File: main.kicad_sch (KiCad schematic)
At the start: 165 parts, among them J1 USB_C_Receptacle_USB2.0_16P, J3 Barrel_Jack_MountingPin, Q1 STL6P3LLH6, Q2 STL6P3LLH6, SW1 TS-1088-AR02016, SW2 TS-1088-AR02016, U1 STUSB4500QTR, U10 INA180A2, U11 INA180A2, U12 INA180A2, U13 INA180A2, U2 LMR16030PDDAR, U3 W25Q128JVS, U5 PCF8575DBR, U6 TPS55289RYQR, U7 ESP32-C3, U8 TPS55289RYQR, U9 AP1117-33, Y1 X322540MPB4SI

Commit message: Schematics done
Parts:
- removed C10, C11, C9: 1uF, Capacitor_SMD:C_0402_1005Metric, symbol Device:C
- removed R7, R8: 100K, PCM_Resistor_SMD_AKL:R_0402_1005Metric, symbol Device:R
- removed TP1: TestPoint, TestPoint:TestPoint_Pad_D1.5mm, symbol Connector:TestPoint
- removed U1: STUSB4500QTR, Package_DFN_QFN:QFN-24-1EP_4x4mm_P0.5mm_EP2.7x2.7mm, symbol Interface_USB:STUSB4500QTR
- removed U5: PCF8575DBR, Package_SO:SSOP-24_5.3x8.2mm_P0.65mm, symbol Interface_Expansion:PCF8575DBR
- added C65, C70, C71: 22uF, Capacitor_SMD:C_0805_2012Metric, symbol Device:C
- added C66, C67, C68: 1uF, Capacitor_SMD:C_0402_1005Metric, symbol Device:C
- added C69, C72: 100nF, Capacitor_SMD:C_0402_1005Metric, symbol Device:C
- added C73, C74: 47uF, Capacitor_SMD:C_0805_2012Metric, symbol Device:C
- added C75, C79, C81: 1uF, Capacitor_SMD:C_0201_0603Metric, symbol Device:C
- added C76, C78, C80, C82: 100nF, Capacitor_SMD:C_0201_0603Metric, symbol Device:C
- added C77: 10uF, Capacitor_SMD:C_0402_1005Metric, symbol Device:C
- added D1, D12, D13, D14, D15, D16, D17, D3: SMBJ40CA, PCM_Diode_SMD_AKL:D_SMB_TVS, symbol PCM_Diode_TVS_AKL:SMBJ40CA
- added D11: SS34, Diode_SMD:D_SMA, symbol PCM_Diode_Schottky_AKL:SS34
- added F1, F6: SL1210650, Fuse:Fuse_1210_3225Metric, symbol Device:Polyfuse
- added F2: SL1210650, symbol Device:Polyfuse
- added F3, F4, F5: SMD1812P350TF, Fuse:Fuse_1812_4532Metric, symbol Device:Polyfuse
- added J4: Conn_01x07_Pin, Connector_PinHeader_1.27mm:PinHeader_1x07_P1.27mm_Vertical, symbol Connector:Conn_01x07_Pin
- added J5: Conn_01x04_Pin, Connector_PinSocket_2.54mm:PinSocket_1x04_P2.54mm_Vertical, symbol Connector:Conn_01x04_Pin
- added J6, J7, J8: Conn_01x11_Pin, Connector_PinHeader_1.27mm:PinHeader_1x11_P1.27mm_Vertical, symbol Connector:Conn_01x11_Pin
- added L6: IHLP4040DZER100M01, Inductor_SMD:L_APV_APH1040, symbol Device:L
- added L7: 2nH, Inductor_SMD:L_0402_1005Metric, symbol Device:L
- added R51: 499, PCM_Resistor_SMD_AKL:R_0201_0603Metric, symbol Device:R
- added R52, R53, R58: 100K, PCM_Resistor_SMD_AKL:R_0402_1005Metric, symbol Device:R
- added R54, R55, R56: 0, PCM_Resistor_SMD_AKL:R_0201_0603Metric, symbol Device:R
- added R57: 49.9K, PCM_Resistor_SMD_AKL:R_0402_1005Metric, symbol Device:R
- added R59: 16.9K, PCM_Resistor_SMD_AKL:R_0402_1005Metric, symbol Device:R
- added R60: 0.01, PCM_Resistor_SMD_AKL:R_0402_1005Metric, symbol Device:R
- added TP17, TP18, TP19, TP20, TP21, TP22, TP23, TP24, TP25: TestPoint, TestPoint:TestPoint_Pad_D1.5mm, symbol Connector:TestPoint
- added TP26, TP27: TestPoint, TestPoint:TestPoint_power, symbol Connector:TestPoint
- added U14: LMR16030PDDAR, LMR16030:LMR16030, symbol LMR16030SDDAR:LMR16030PDDAR
- added U4: PCA9555PW, Package_SO:TSSOP-24_4.4x7.8mm_P0.65mm, symbol Interface_Expansion:PCA9555PW
- added U5: STUSB4500QTR, Package_DFN_QFN:QFN-24-1EP_4x4mm_P0.5mm_EP2.7x2.7mm, symbol Interface_USB:STUSB4500QTR
- J1: value USB_C_Receptacle_USB2.0_16P -> TYPE-C-31-M-31
- J3: value Barrel_Jack_MountingPin -> DC-005-5A-2.5-SMT
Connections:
- net +3.3V_LDO: now also U7.11 (VDD3P3_RTC), U7.17 (VDD3P3_CPU), U7.18 (VDD_SPI), U7.31 (VDDA), U7.32 (VDDA), C69.1, C76.1, C77.1, C78.1, C79.1, C80.1, C81.1, C82.1, J5.1 (Pin_1), J7.1 (Pin_1), J7.10 (Pin_10), J7.11 (Pin_11), J7.2 (Pin_2), J7.3 (Pin_3), J7.4 (Pin_4), J7.5 (Pin_5), J7.6 (Pin_6), J7.7 (Pin_7), J7.8 (Pin_8), J7.9 (Pin_9), L7.1, TP22.1, U4.24 (VDD)
- net +5.2V: now also F4.1; no longer C47.1, TP10.1, U13.4 (-), U9.3 (VI)
- net +5.2V_: now also C65.1, J4.6 (Pin_6); no longer C43.1, C44.1, L3.2, R20.1, R23.1, U13.3 (+)
- net +5V_USB: now also D16.2 (A)
- net DISH: now also U5.9 (DISCH)
- net Earth: now also J3.MP (MountPin), C65.2, C66.2, C67.2, C68.2, C69.2, C70.2, C71.2, C73.2, C74.2, C75.2, C76.2, C77.2, C78.2, C79.2, C80.2, C81.2, C82.2, D1.1 (K), D11.2 (A), D12.1 (K), D13.1 (K), D14.1 (K), D15.1 (K), D16.1 (K), D17.1 (K), D3.1 (K), J4.7 (Pin_7), J5.4 (Pin_4), J8.1 (Pin_1), J8.10 (Pin_10), J8.11 (Pin_11), J8.2 (Pin_2), J8.3 (Pin_3), J8.4 (Pin_4), J8.5 (Pin_5), J8.6 (Pin_6), J8.7 (Pin_7), J8.8 (Pin_8), J8.9 (Pin_9), R52.2, R53.2, R54.1, R55.1, R56.1, R57.2, R59.2, TP21.1, TP27.1, U14.7 (GND), U14.9 (EP), U4.12 (VSS), U5.10 (GND), U5.22 (VSYS), U5.25 (GND), U5.3 (NC)
- net LDO_EN: now also U4.7 (IO0_3)
- net PD-RST: now also U4.6 (IO0_2), U5.6 (RESET)
- net PD-Voltage: now also C70.1, C71.1, D17.2 (A), F6.1, U14.2 (VIN), U14.3 (EN); no longer TP15.1
- net PD_VDD: now also C68.1, U5.24 (VDD)
- net SCL: now also TP18.1, U4.22 (SCL), U5.7 (SCL)
- net SDA: now also TP17.1, U4.23 (SDA), U5.8 (SDA)
- net SPI_MOSI: now also J4.4 (Pin_4), TP19.1
- net SPI_SCLK: now also J4.5 (Pin_5), TP20.1
- net ST7789_CS: now also J4.1 (Pin_1)
- net ST7789_DC: now also J4.2 (Pin_2)
- net TPS1_EN: now also U4.4 (IO0_0)
- net TPS2_EN: now also U4.5 (IO0_1)
- net U0RX: now also J5.2 (Pin_2)
- net U0TX: now also R51.2
- net VBUS_EN_SNK: now also U5.16 (VBUS_EN_SNK)
- net VBUS_VS_DISH: now also U5.18 (VBUS_VS_DISCH)
- net VOUT1: now also F1.1; no longer TP7.1
- net VOUT2: now also F2.1; no longer TP8.1
- net VOUT3: now also F3.1; no longer TP9.1
- net at D4.1 (L1), J1.A5 (CC1): now also U5.1 (CC1DB), U5.2 (CC1)
- net at D4.3 (L2), J1.B5 (CC2): now also U5.4 (CC2), U5.5 (CC2DB)
- net at U7.2 (VDD3P3): now also U7.3 (VDD3P3), C75.1, L7.2
- new net: D13.2 (A), F4.2, TP10.1
- new net: C66.1, U5.23 (VREG_2V7)
- new net: R58.2, R59.1, U14.5 (FB)
- new net: D14.2 (A), F5.2, TP26.1
- new net: C43.1, C44.1, L3.2, R20.1, R23.1
- new net: C67.1, U5.21 (VREG_1V2)
- new net: C72.1, U14.1 (BOOT)
- new net: C72.2, D11.1 (K), L6.1, U14.8 (SW)
- new net: D3.2 (A), F2.2, TP8.1
- new net: TP24.1, U4.1 (~{INT})
- new net: R52.1, U5.12 (ADDR0)
- new net: R53.1, U5.13 (ADDR1)
- new net: TP23.1, U5.19 (ALERT)
- new net: R55.2, U4.2 (A1)
- new net: R57.1, U14.4 (RT/SYNC)
- new net: D12.2 (A), F3.2, TP9.1
- new net: R56.2, U4.21 (A0)
- new net: D15.2 (A), F6.2, TP15.1
- new net: TP25.1, U14.6 (PG)
- new net: J5.3 (Pin_3), R51.1
- new net: R54.2, U4.3 (A2)
- new net: D1.2 (A), F1.2, TP7.1
- new net +5.2V_USB: F5.1, R60.2, U13.4 (-)
- new net +5.2V_USB_: C47.1, C73.1, C74.1, L6.2, R58.1, R60.1, U13.3 (+), U9.3 (VI)
- new net BUTTON_1: J6.1 (Pin_1), U4.9 (IO0_5)
- new net BUTTON_10: J6.10 (Pin_10), U4.19 (IO1_6)
- new net BUTTON_11: J6.11 (Pin_11), U4.20 (IO1_7)
- new net BUTTON_2: J6.2 (Pin_2), U4.10 (IO0_6)
- new net BUTTON_3: J6.3 (Pin_3), U4.11 (IO0_7)
- new net BUTTON_4: J6.4 (Pin_4), U4.13 (IO1_0)
- new net BUTTON_5: J6.5 (Pin_5), U4.14 (IO1_1)
- new net BUTTON_6: J6.6 (Pin_6), U4.15 (IO1_2)
- new net BUTTON_7: J6.7 (Pin_7), U4.16 (IO1_3)
- new net BUTTON_8: J6.8 (Pin_8), U4.17 (IO1_4)
- new net BUTTON_9: J6.9 (Pin_9), U4.18 (IO1_5)
- new net ST7789_RST: J4.3 (Pin_3), U4.8 (IO0_4)
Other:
- note added: "1"
- note added: "2"
- note added: "3"
- note added: "4"
- note added: "5"
- note added: "6"
- note added: "OUTPUT"
- note removed: "1)Подключить выключатели питания для 3х доменов а также общий выключатель без которого бы не было б управления 2)добавить внешние коннекторы для дисплея и кнопок 3)Добавить тестпоинты на I2C и SPI шины 4)Вывести и неиспользуемые пины расширителя пинов 5)Поставить неиспользуемый второй модуль расширения пинов но уже с другим адресом и выводом на тестовые пины - как бы на вырост"
- moved on the sheet: AE1, C1, C12, C13, C14, C15, C16, C17, C18, C19, C2, C20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

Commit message: upd library + PCB created
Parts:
- removed J3: DC-005-5A-2.5-SMT, Connector_BarrelJack:BarrelJack_GCT_DCJ200-10-A_Horizontal, symbol Connector:Barrel_Jack_MountingPin
- added J1: DC-005-5A-2.5-SMT, DC-005-5A:DC-005-5A, symbol DC-005-5A-2_5-SMT:DC-005-5A-2.5-SMT
- F3: renamed from F2; footprint (none) -> Fuse:Fuse_1210_3225Metric
- renumbered C61 to C1, C48 to C10, C49 to C11, C50 to C12, C69 to C13, C82 to C14, C80 to C15, C64 to C16, C81 to C17, C63 to C18, C66 to C19, C77 to C2, C67 to C20, C68 to C21, C7 to C22, C6 to C23, C5 to C24, C4 to C25, C62 to C26, C56 to C27, C57 to C28, C3 to C29, C65 to C3, C58 to C30, C59 to C31, C51 to C32, C52 to C33, C21 to C34, C22 to C35, C55 to C36, C20 to C37, C23 to C38, C19 to C39, C76 to C4, C24 to C40, C18 to C41, C25 to C42, C1 to C43, C26 to C44, C70 to C46, C46 to C47, C71 to C48, C36 to C49, C60 to C5, C37 to C50, C2 to C51, C27 to C52, C8 to C53, C28 to C54, C35 to C55, C72 to C56, C12 to C57, C29 to C58, C40 to C59, C75 to C6, C42 to C60, C13 to C61, C30 to C62, C15 to C63, C31 to C64, C41 to C65, C14 to C66, C16 to C67, C32 to C68, C33 to C69, C47 to C7, C43 to C70, C73 to C71, C38 to C72, C53 to C73, C44 to C74, C74 to C75, C39 to C76, C54 to C77, C17 to C78, C34 to C79, C78 to C8, C79 to C9, D16 to D1, D6 to D10, D15 to D12, D1 to D13, D3 to D14, D12 to D15, D13 to D16, D14 to D17, D17 to D2, D4 to D3, D7 to D4, D8 to D5, D9 to D6, D10 to D7, D2 to D8, D5 to D9, F6 to F1, F1 to F2, F3 to F4, F4 to F5, F5 to F6, J4 to J2, J5 to J3, J1 to J4, J6 to J5, J7 to J6, J8 to J7, L7 to L1, L4 to L2, L5 to L3, L1 to L4, L2 to L5, L3 to L6, L6 to L7, R43 to R1, R45 to R10, R46 to R11, R47 to R12, R48 to R13, R50 to R14, R24 to R15, R52 to R16, R25 to R17, R53 to R18, R26 to R19, R42 to R2, R27 to R20, R28 to R21, R29 to R22, R30 to R23, R31 to R24, R32 to R25, R33 to R26, R56 to R27, R55 to R28, R54 to R29, R51 to R3, R44 to R30, R35 to R31, R4 to R32, R5 to R33, R49 to R35, R2 to R36, R1 to R37, R3 to R38, R6 to R39, R40 to R4, R13 to R40, R14 to R41, R11 to R42, R15 to R43, R19 to R44, R57 to R45, R12 to R46, R16 to R47, R10 to R48, R17 to R49, R41 to R5, R9 to R50, R18 to R51, R20 to R52, R21 to R53, R58 to R54, R59 to R55, R22 to R56, R23 to R57, R60 to R58, R39 to R6, R38 to R7, R37 to R8, R36 to R9, SW2 to SW1, SW1 to SW2, TP22 to TP1, TP25 to TP10, TP2 to TP11, TP3 to TP12, TP4 to TP13, TP5 to TP14, TP7 to TP17, TP11 to TP18, TP8 to TP19, TP17 to TP2, TP12 to TP20, TP9 to TP21, TP13 to TP22, TP10 to TP23, TP14 to TP24, TP26 to TP25, TP27 to TP26, TP18 to TP3, TP19 to TP4, TP20 to TP5, TP21 to TP6, TP23 to TP7, TP24 to TP8, TP6 to TP9, U9 to U1, U6 to U10, U8 to U11, U2 to U12, U14 to U13, U7 to U2, U5 to U3, U3 to U5, U10 to U6, U11 to U7, U12 to U8, U13 to U9
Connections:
- net Earth: now also J1.2, J1.3
- net PD-Voltage: now also J1.A1, J1.B1
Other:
- moved on the sheet: D2, D4, D5, D6, D7, R15, R17, R19, R20

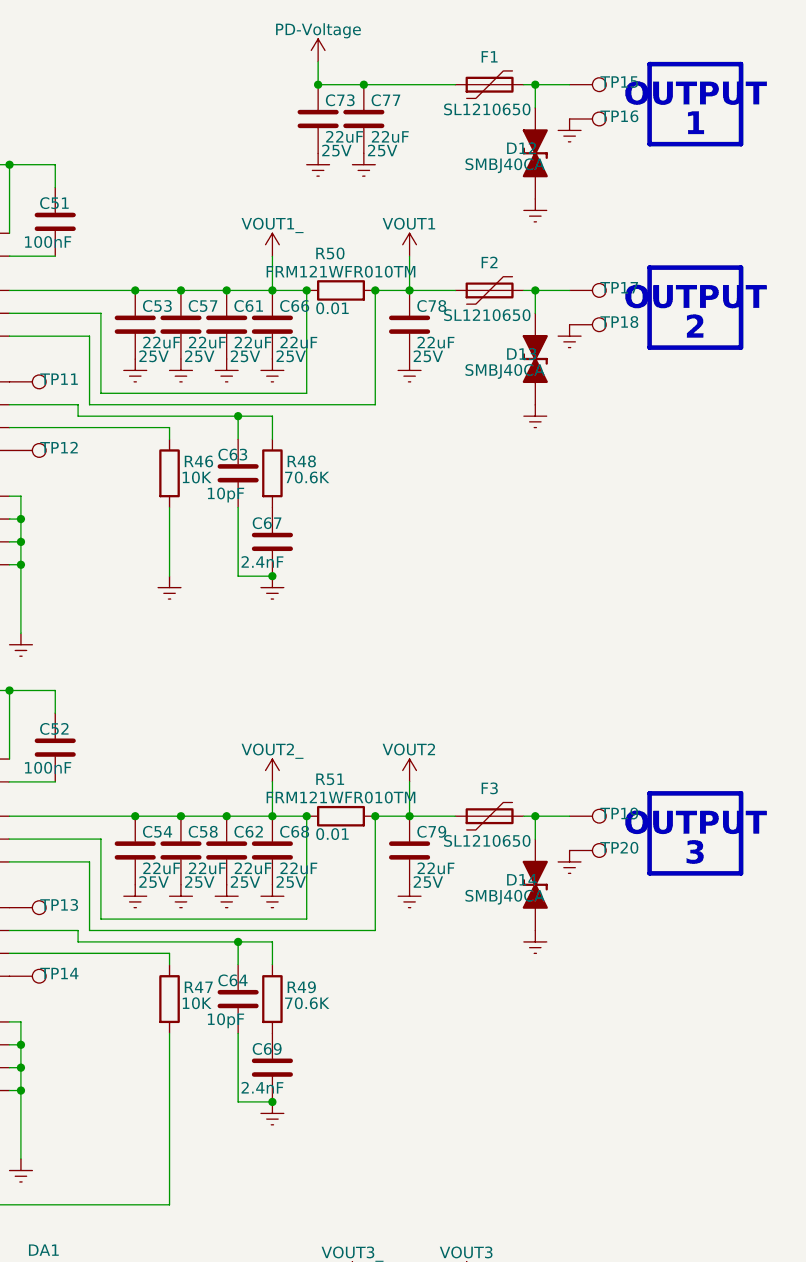
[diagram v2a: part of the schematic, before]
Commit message: Added JLCPCB BOM + placed main components on PCB to form a prototype
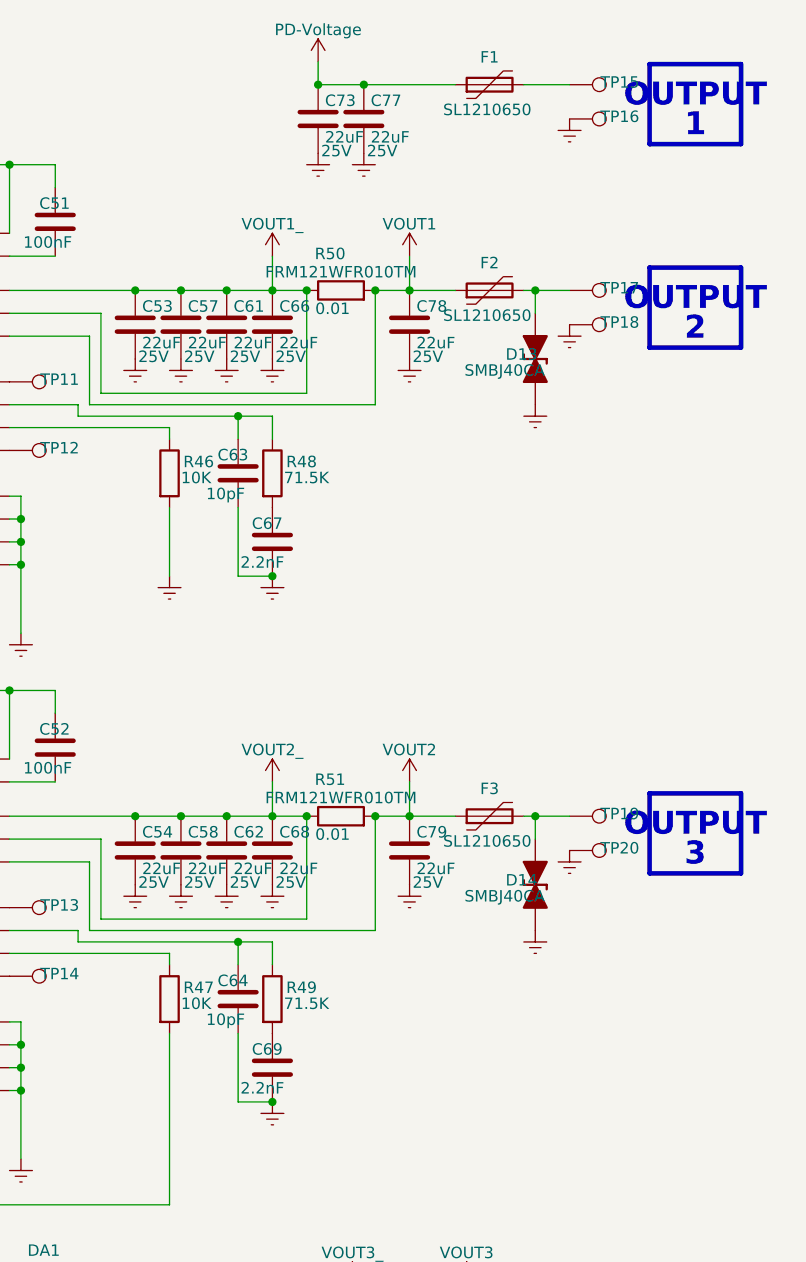
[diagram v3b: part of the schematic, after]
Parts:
- removed D12: SMBJ40CA, PCM_Diode_SMD_AKL:D_SMB_TVS, symbol PCM_Diode_TVS_AKL:SMBJ40CA
- C67, C69: value 2.4nF -> 2.2nF
- R48, R49: value 70.6K -> 71.5K
- R50, R51, R56, R57, R58: footprint PCM_Resistor_SMD_AKL:R_0402_1005Metric -> Resistor_SMD:R_1206_3216Metric

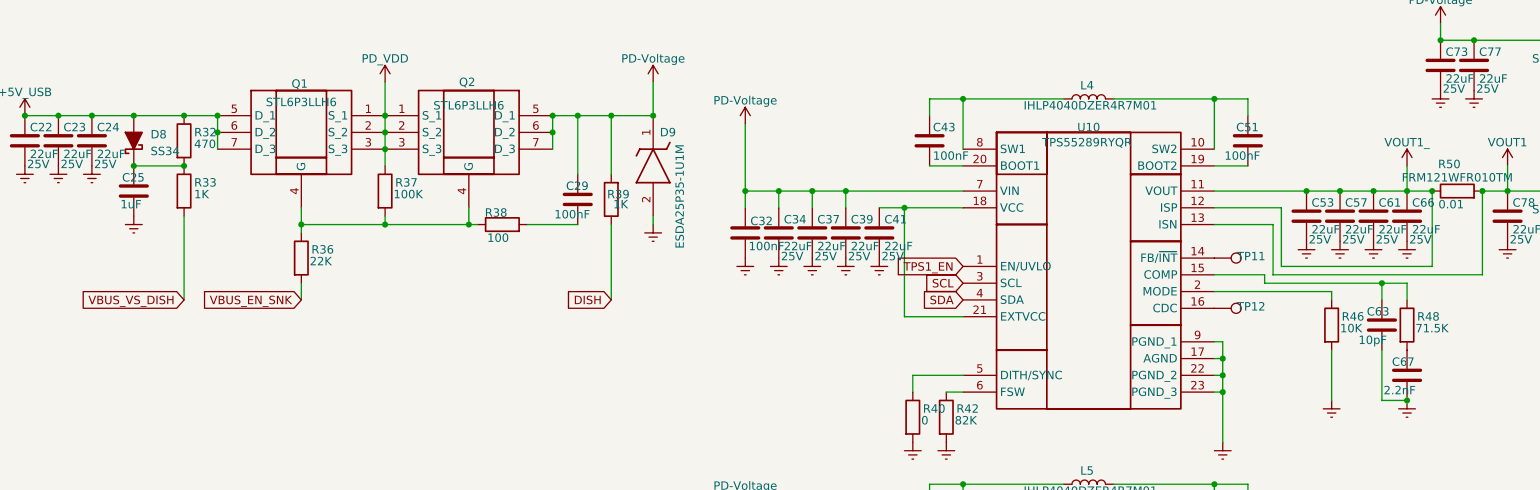
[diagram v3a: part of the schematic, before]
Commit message: Finished components placement + silkscreen placement Reviewed schematics, changed outline Ready for tracing
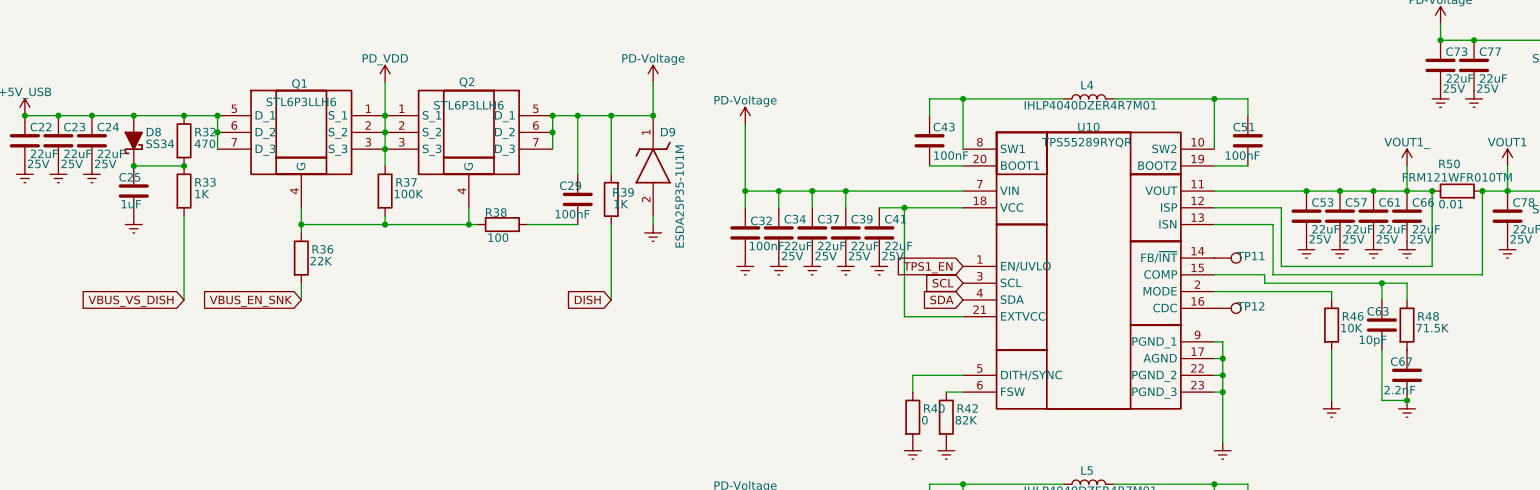
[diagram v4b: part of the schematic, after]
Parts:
- R1, R2: footprint PCM_Resistor_SMD_AKL:R_0402_1005Metric -> PCM_Resistor_SMD_AKL:R_0201_0603Metric

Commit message: Finished rev0
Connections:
- net BUTTON_1: now also U4.6 (IO0_2); no longer U4.9 (IO0_5)
- net BUTTON_2: now also U4.5 (IO0_1); no longer U4.10 (IO0_6)
- net BUTTON_3: now also U4.4 (IO0_0); no longer U4.11 (IO0_7)
- net LDO_EN: now also U4.8 (IO0_4); no longer U4.7 (IO0_3)
- net PD-RST: now also U4.9 (IO0_5); no longer U4.6 (IO0_2)
- net ST7789_RST: now also U4.7 (IO0_3); no longer U4.8 (IO0_4)
- net TPS1_EN: now also U4.11 (IO0_7); no longer U4.4 (IO0_0)
- net TPS2_EN: now also U4.10 (IO0_6); no longer U4.5 (IO0_1)
